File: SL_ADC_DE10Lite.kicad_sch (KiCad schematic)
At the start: 23 parts, among them J1 DE10Lite header, J2 Analog header

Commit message: updated?
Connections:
- net DGND is gone; now on net AGND: C5.2, IC1.24 (DGND), J1.12 (Pin_12), J1.30 (Pin_30), J2.27 (Pin_27), J2.28 (Pin_28)
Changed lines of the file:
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@@
+	(wire
+		(pts
+			(xy 93.98 96.52) (xy 100.33 96.52)
+		)
+		(stroke
+			(width 0)
+			(type default)
+		)
+	)
 	(wire
 		(pts
@@
 		)
 	)
+	(label "AGND"
+		(at 93.98 96.52 180)
+		(effects
+			(font
+				(size 1.27 1.27)
+			)
+			(justify right bottom)
+		)
+	)
 	(label "AVDD"
 		(at 43.18 74.93 180)
@@
 		)
 	)
+	(label "DGND"
+		(at 100.33 96.52 0)
+		(effects
+			(font
+				(size 1.27 1.27)
+			)
+			(justify left bottom)
+		)
+	)

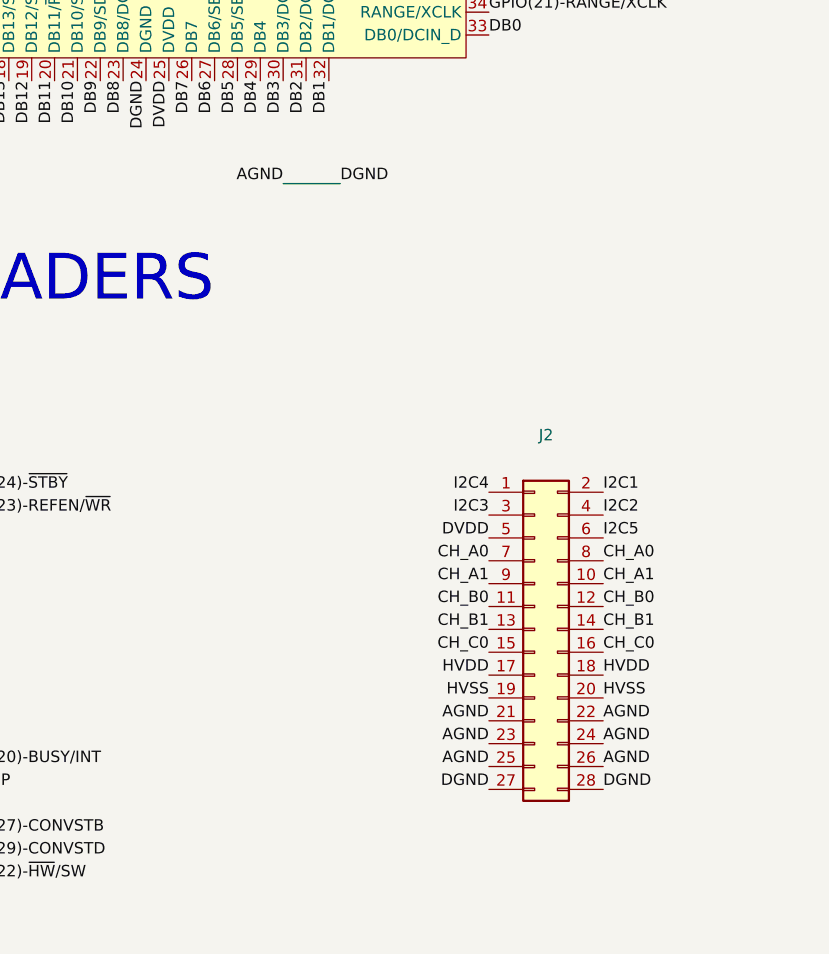
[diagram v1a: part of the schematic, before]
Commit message: widened standoff holes
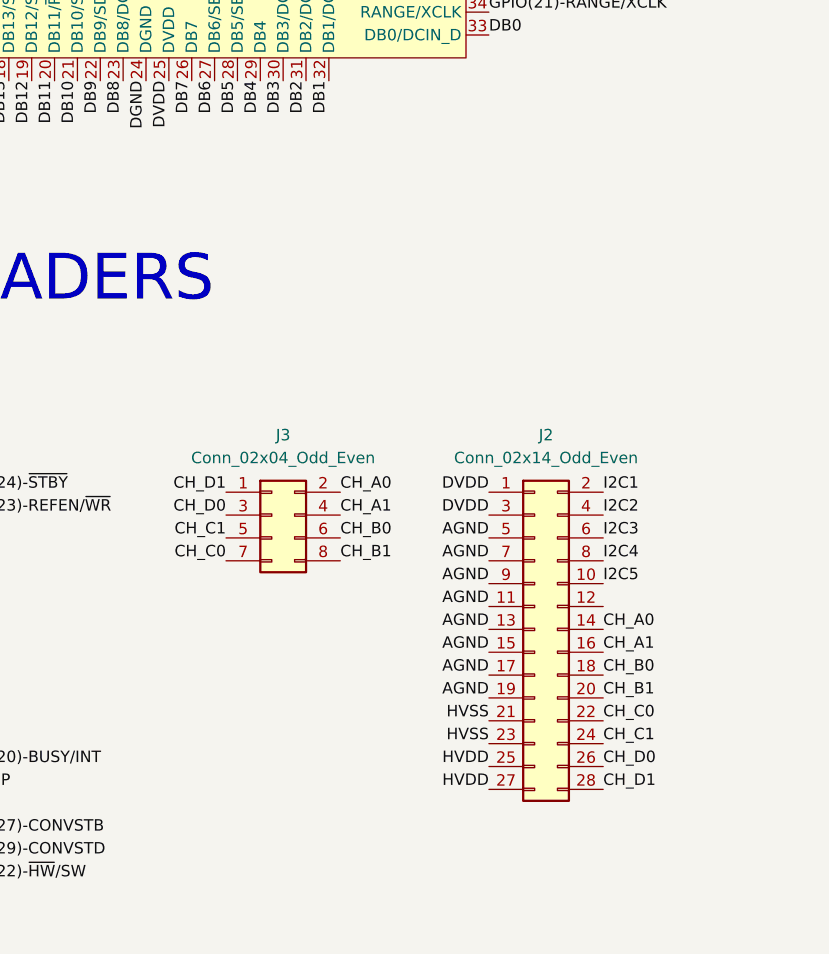
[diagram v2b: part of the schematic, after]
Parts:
- added J3: Conn_02x04_Odd_Even, Connector_PinHeader_2.54mm:PinHeader_2x04_P2.54mm_Horizontal, symbol Connector_Generic:Conn_02x04_Odd_Even
- J2: value Analog header -> Conn_02x14_Odd_Even
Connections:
- net AGND: now also J2.11 (Pin_11), J2.13 (Pin_13), J2.15 (Pin_15), J2.17 (Pin_17), J2.19 (Pin_19), J2.5 (Pin_5), J2.7 (Pin_7), J2.9 (Pin_9); no longer C5.2, IC1.24 (DGND), J1.12 (Pin_12), J1.30 (Pin_30), J2.21 (Pin_21), J2.22 (Pin_22), J2.23 (Pin_23), J2.24 (Pin_24), J2.25 (Pin_25), J2.26 (Pin_26), J2.27 (Pin_27), J2.28 (Pin_28)
- net CH_A0: now also J2.14 (Pin_14), J3.2 (Pin_2); no longer J2.7 (Pin_7), J2.8 (Pin_8)
- net CH_A1: now also J2.16 (Pin_16), J3.4 (Pin_4); no longer J2.10 (Pin_10), J2.9 (Pin_9)
- net CH_B0: now also J2.18 (Pin_18), J3.6 (Pin_6); no longer J2.11 (Pin_11), J2.12 (Pin_12)
- net CH_B1: now also J2.20 (Pin_20), J3.8 (Pin_8); no longer J2.13 (Pin_13), J2.14 (Pin_14)
- net CH_C0: now also J2.22 (Pin_22), J3.7 (Pin_7); no longer J2.15 (Pin_15), J2.16 (Pin_16)
- net CH_C1: now also J2.24 (Pin_24), J3.5 (Pin_5)
- net CH_D0: now also J2.26 (Pin_26), J3.3 (Pin_3)
- net CH_D1: now also J2.28 (Pin_28), J3.1 (Pin_1)
- net DVDD: now also J2.1 (Pin_1), J2.3 (Pin_3); no longer J2.5 (Pin_5)
- net HVDD: now also J2.25 (Pin_25), J2.27 (Pin_27); no longer J2.17 (Pin_17), J2.18 (Pin_18)
- net HVSS: now also J2.21 (Pin_21), J2.23 (Pin_23); no longer J2.19 (Pin_19), J2.20 (Pin_20)
- net I2C3: now also J2.6 (Pin_6); no longer J2.3 (Pin_3)
- net I2C4: now also J2.8 (Pin_8); no longer J2.1 (Pin_1)
- net I2C5: now also J2.10 (Pin_10); no longer J2.6 (Pin_6)
- new net DGND: C5.2, IC1.24 (DGND), J1.12 (Pin_12), J1.30 (Pin_30)
